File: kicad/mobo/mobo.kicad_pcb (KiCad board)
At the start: 4 copper layers, 22 x 58 mm, 47 parts, among them J1 HRO_TYPE-C-31-M-14, J2 Battery, J3 rgb, J4 columns, J5 Conn_01x10, J6 rows, J7 sensor, Q1 AO3401A, Q2 2N7002, SW1 Battery, SW2 Reset, U1 BQ24075, U2 nRF52840_E73-2G4M08S1C, Y1 32.768 KHz

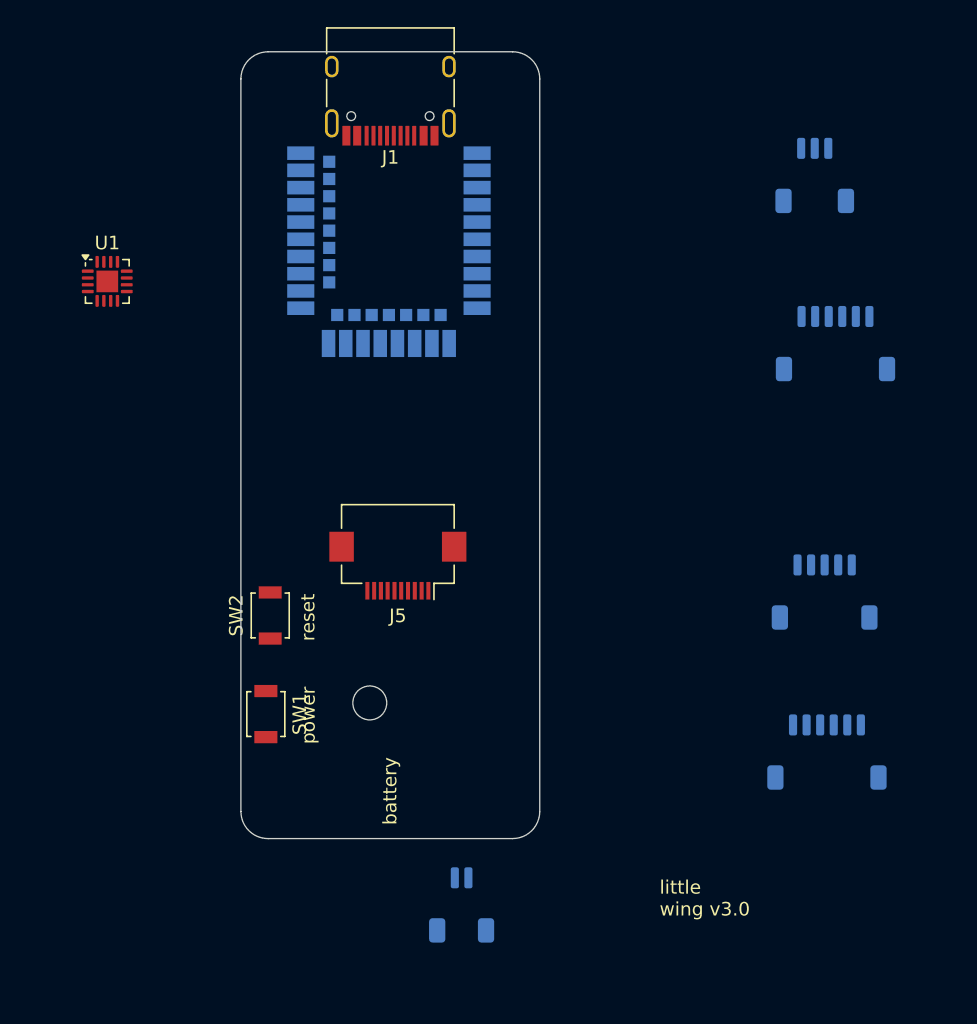
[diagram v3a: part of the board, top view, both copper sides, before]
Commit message: Adding connectors 3d files
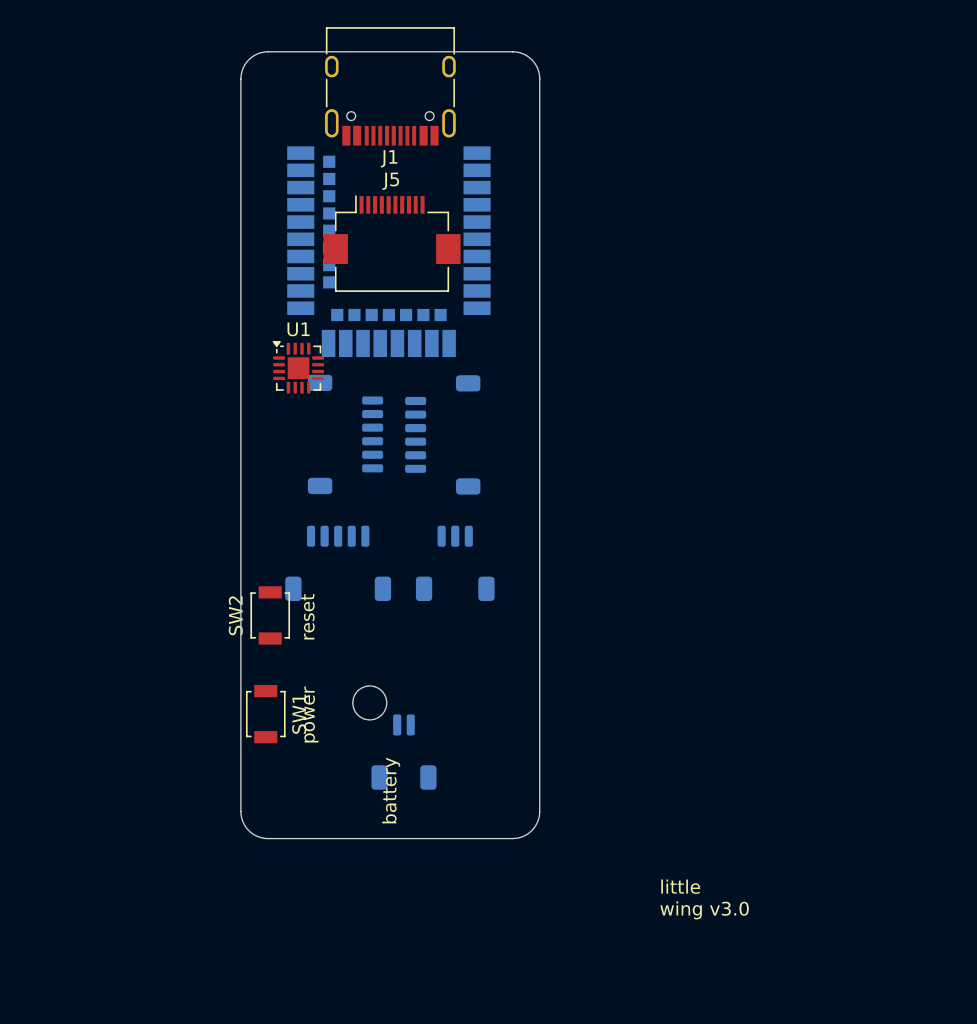
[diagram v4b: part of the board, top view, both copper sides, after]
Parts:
- moved J7 42.5 mm to (189.8, 60.2), turned to 90 degrees
- moved J3 39.0 mm to (197.8, 69.7)
- moved J6 35.9 mm to (189.2, 69.7)
- moved J4 29.7 mm to (196.9, 60.2), turned to -90 degrees
- moved J5 24.7 mm to (193.2, 45.1), turned to 0 degrees
- moved U1 15.5 mm to (186.3, 55.3)
- moved J2 12.0 mm to (194.1, 83.6)

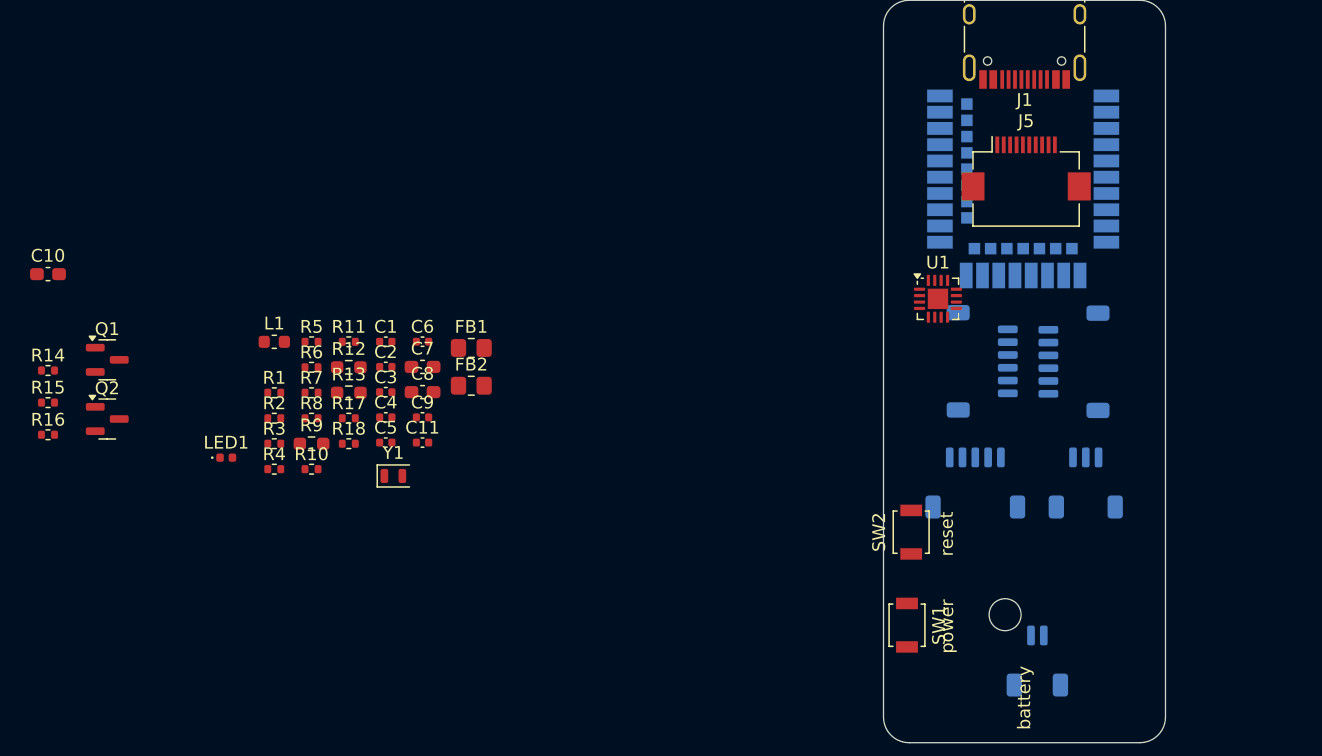
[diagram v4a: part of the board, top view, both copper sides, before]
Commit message: Assigning all the perifery pins
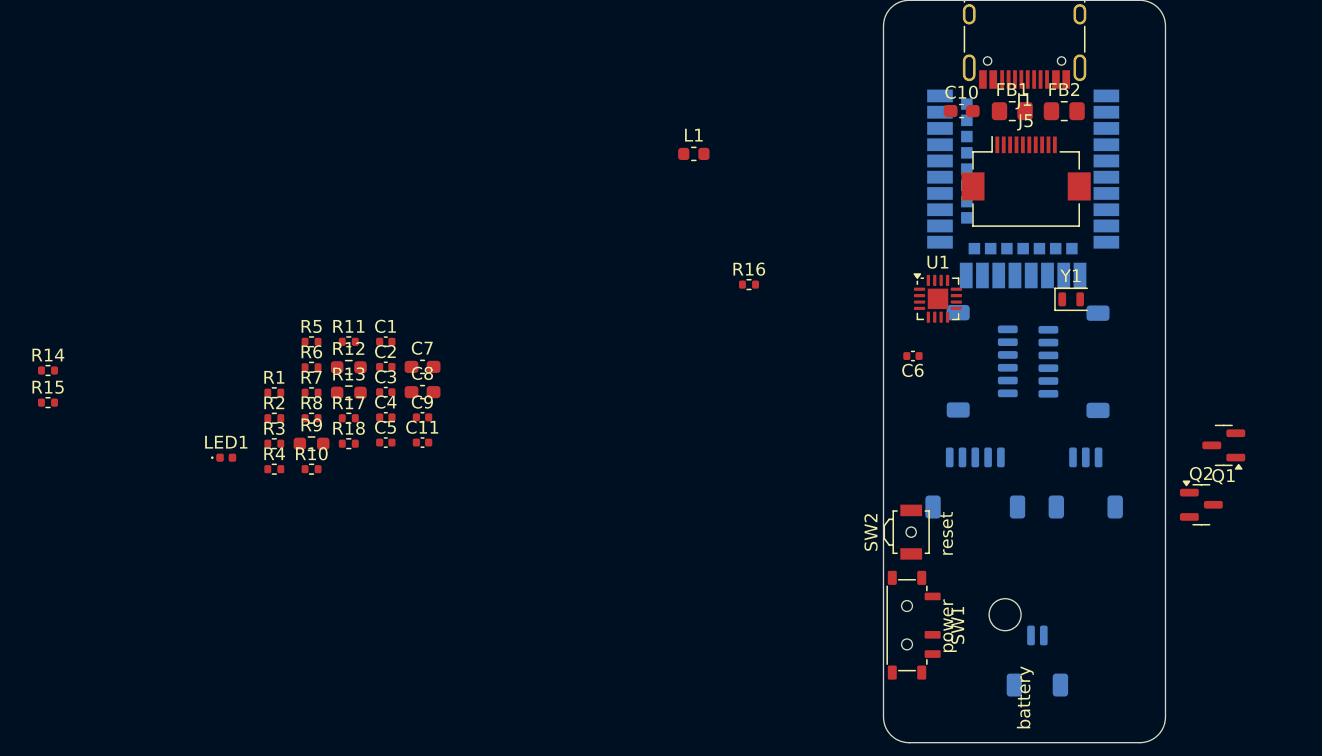
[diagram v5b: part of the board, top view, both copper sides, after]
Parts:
- SW1: footprint Button_Switch_SMD:SW_SPST_B3U-1000P -> ScottoKeebs_Components:Switch_MSK12C02
- SW2: footprint Button_Switch_SMD:SW_SPST_B3U-1000P -> Button_Switch_SMD:SW_SPST_B3U-3000P-B
- moved Q1 87.5 mm to (208.6, 66.8), turned to 180 degrees
- moved Q2 85.7 mm to (206.9, 71.4)
- moved C10 72.5 mm to (188.1, 40.7)
- moved R16 56.0 mm to (171.5, 54.2)
- moved Y1 54.7 mm to (196.7, 55.4)
- moved FB2 51.1 mm to (196.2, 40.7)
- moved FB1 46.1 mm to (192.1, 40.7)
- moved C6 38.3 mm to (184.3, 59.8), turned to 180 degrees
- moved L1 35.9 mm to (167.2, 44.0)
- turned SW1 to 90 degrees

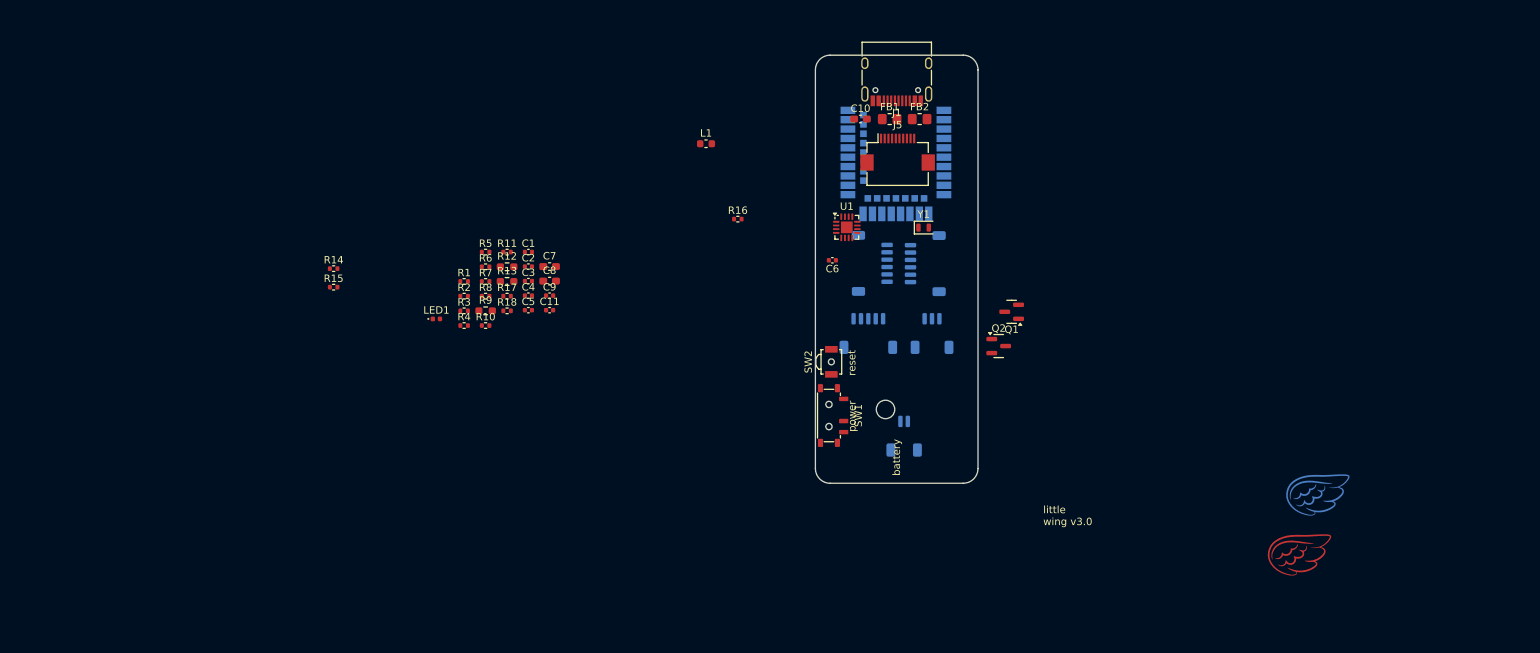
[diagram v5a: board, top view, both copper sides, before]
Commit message: Groupping around the PCB components
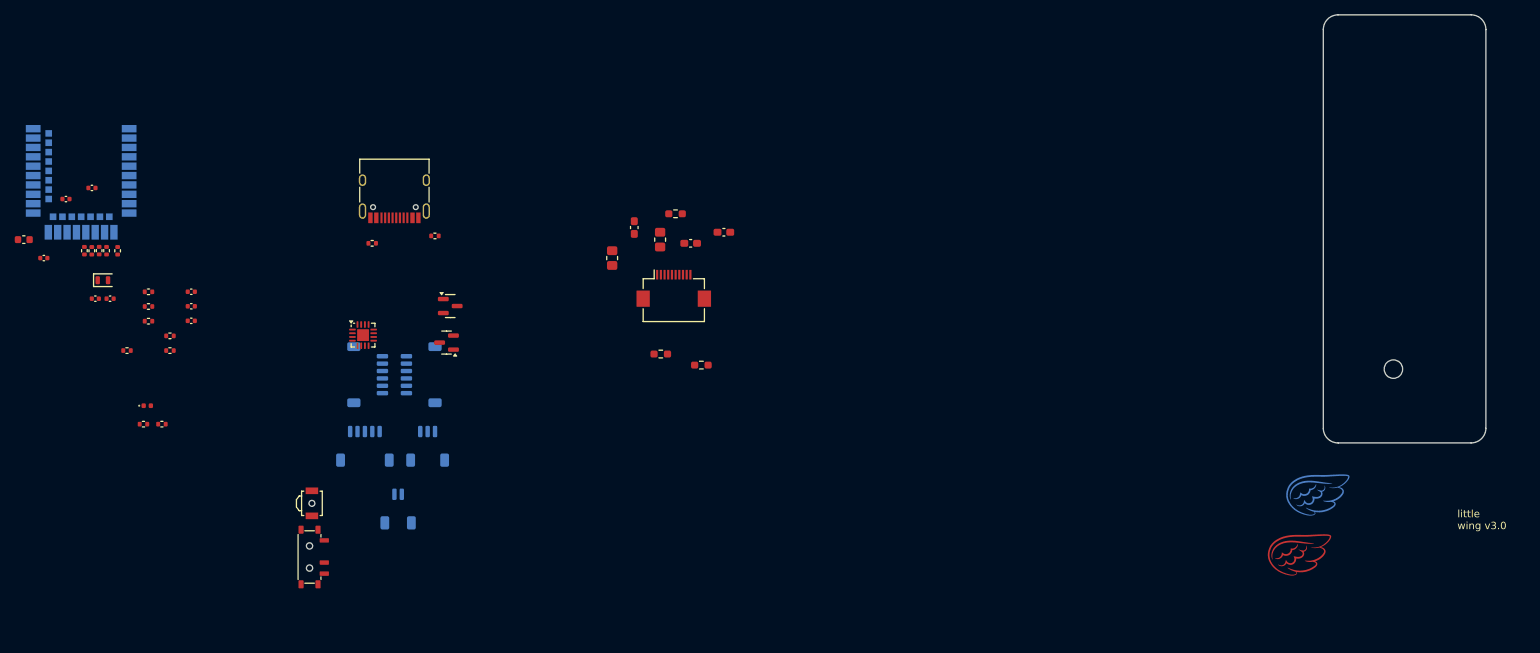
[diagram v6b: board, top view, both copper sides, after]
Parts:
- moved Y1 111.4 mm to (85.5, 62.5)
- moved U2 110.4 mm to (82.6, 47.0)
- moved C6 104.2 mm to (80.5, 51.5)
- moved L1 93.3 mm to (74.8, 57.0)
- moved R16 88.6 mm to (83.0, 58.5), turned to -90 degrees
- moved J4 77.0 mm to (121.4, 75.3), turned to 90 degrees
- moved Q1 76.7 mm to (132.1, 71.0)
- moved Q2 74.5 mm to (132.6, 66.0)
- moved SW1 72.9 mm to (113.5, 100.0)
- moved SW2 72.9 mm to (113.8, 92.7)
- moved J3 70.0 mm to (129.5, 85.0)
- moved J6 69.9 mm to (121.0, 85.0)
- moved J1 69.9 mm to (125.0, 50.0)
- moved J2 69.3 mm to (125.5, 93.5)
- moved U1 67.2 mm to (120.8, 69.9)
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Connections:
- J5 pad 2: LCD_IN -> LCD_DATA
- R11 pad 1: SESOR_CS -> SENSOR_CS
- R15 pad 1: SENSOR_SCK -> SENSOR_CLK
- U2 pad 12: unconnected-(U2-P0.26-Pad12) -> LCD_CS
- U2 pad 14: unconnected-(U2-P0.06-Pad14) -> LCD_DATA
- U2 pad 15: unconnected-(U2-P0.05/AIN3-Pad15) -> LCD_CLK
- U2 pad 16: unconnected-(U2-P0.08-Pad16) -> SENSOR_CS
- U2 pad 18: unconnected-(U2-P0.04/AIN2-Pad18) -> SENSOR_SDIO
- U2 pad 20: unconnected-(U2-P0.12-Pad20) -> SENSOR_CLK
- U2 pad 22: unconnected-(U2-P0.07-Pad22) -> SENSOR_IRQ
- U2 pad 28: unconnected-(U2-P0.15-Pad28) -> Row 5
- U2 pad 30: unconnected-(U2-P0.17-Pad30) -> Row 4
- U2 pad 32: unconnected-(U2-P0.20-Pad32) -> Row 3
- U2 pad 33: unconnected-(U2-P0.13-Pad33) -> Row 2
- U2 pad 34: unconnected-(U2-P0.22-Pad34) -> Row 1
- U2 pad 35: unconnected-(U2-P0.24-Pad35) -> Row 0
- U2 pad 36: RGB_ON -> Col 5
- U2 pad 38: unconnected-(U2-P1.02-Pad38) -> Col 4
- U2 pad 40: unconnected-(U2-P1.04-Pad40) -> Col 3
- U2 pad 41: unconnected-(U2-P0.09/NFC1-Pad41) -> Col 2
- U2 pad 42: unconnected-(U2-P1.06-Pad42) -> Col 1
- U2 pad 43: unconnected-(U2-P0.10/NFC2-Pad43) -> Col 0
- U2 pad 7: unconnected-(U2-P0.02/AIN0-Pad7) -> RGB_DATA
- U2 pad 8: unconnected-(U2-P0.29/AIN5-Pad8) -> RGB_ON
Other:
- board text removed: "battery"
- board text removed: "power"
- board text removed: "reset"

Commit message: Loosely optimising the groups components placement
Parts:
- added SW1: Battery, ScottoKeebs_Components:Switch_MSK12C02, F.Cu at (134.0, 100.0)
- added SW2: Reset, Button_Switch_SMD:SW_SPST_B3U-3000P-B, F.Cu at (134.0, 92.7)
- FB1, FB2: value Ferrite_Bead_Small -> 2.7k; footprint Resistor_SMD:R_0805_2012Metric_Pad1.20x1.40mm_HandSolder -> Resistor_SMD:R_0603_1608Metric
- R12, R13, R9: footprint Resistor_SMD:R_0603_1608Metric_Pad0.98x0.95mm_HandSolder -> Resistor_SMD:R_0402_1005Metric
- moved R2 56.9 mm to (76.0, 40.0)
- moved R10 53.3 mm to (146.5, 76.5), turned to -90 degrees
- moved R18 52.5 mm to (146.5, 80.0), turned to 90 degrees
- moved J1 44.6 mm to (82.5, 36.5)
- moved R1 37.3 mm to (89.0, 40.0)
- moved U1 24.3 mm to (96.4, 68.8)
- moved R17 20.0 mm to (87.0, 51.5), turned to -90 degrees
- moved Q2 18.2 mm to (144.1, 80.0), turned to 180 degrees
- moved C7 14.6 mm to (162.0, 68.5), turned to -90 degrees
- moved R9 14.5 mm to (163.5, 68.0), turned to 90 degrees
- moved FB1 13.8 mm to (165.0, 68.5), turned to -90 degrees
- moved R4 13.8 mm to (100.0, 71.5)
- moved C10 13.2 mm to (156.0, 68.5), turned to -90 degrees
- moved Q1 13.2 mm to (144.1, 76.5)
- moved C8 11.9 mm to (160.5, 68.5), turned to -90 degrees
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
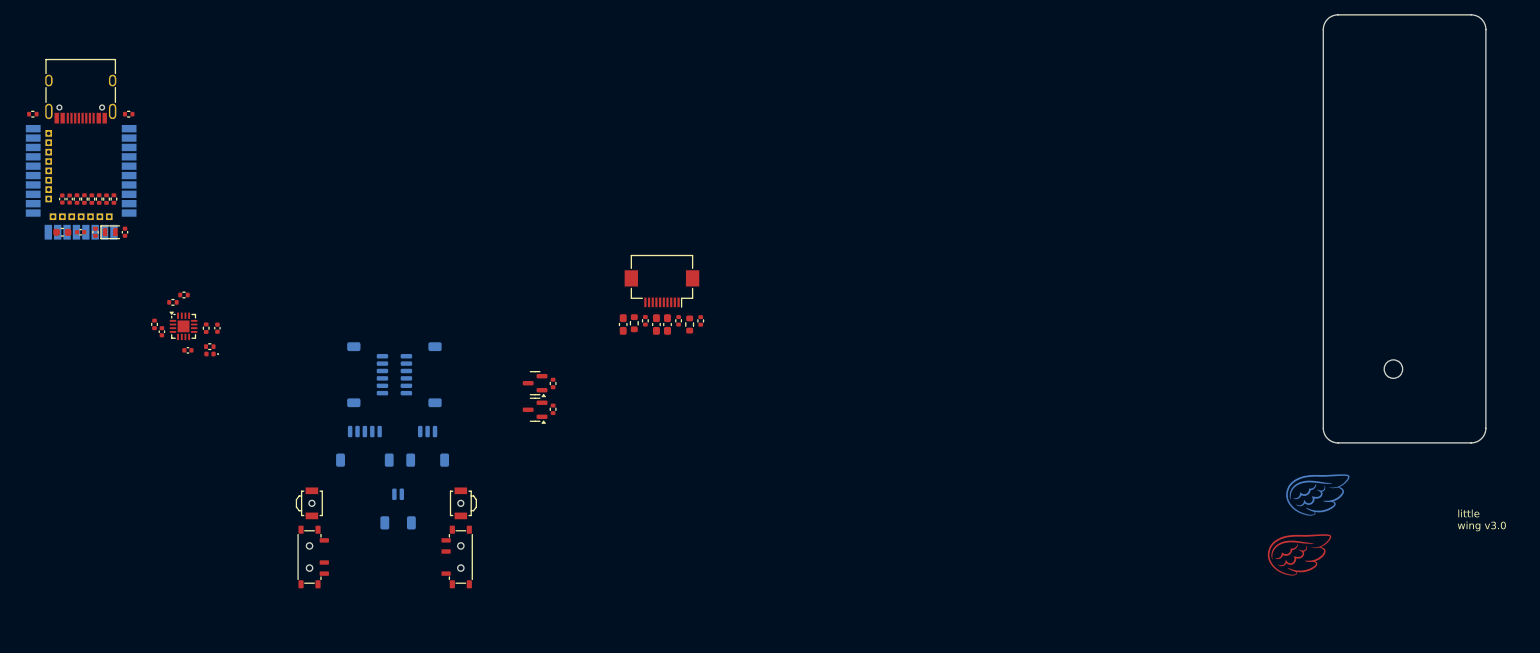
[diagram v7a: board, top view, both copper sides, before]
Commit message: Groupping the groups into a workable arrangement
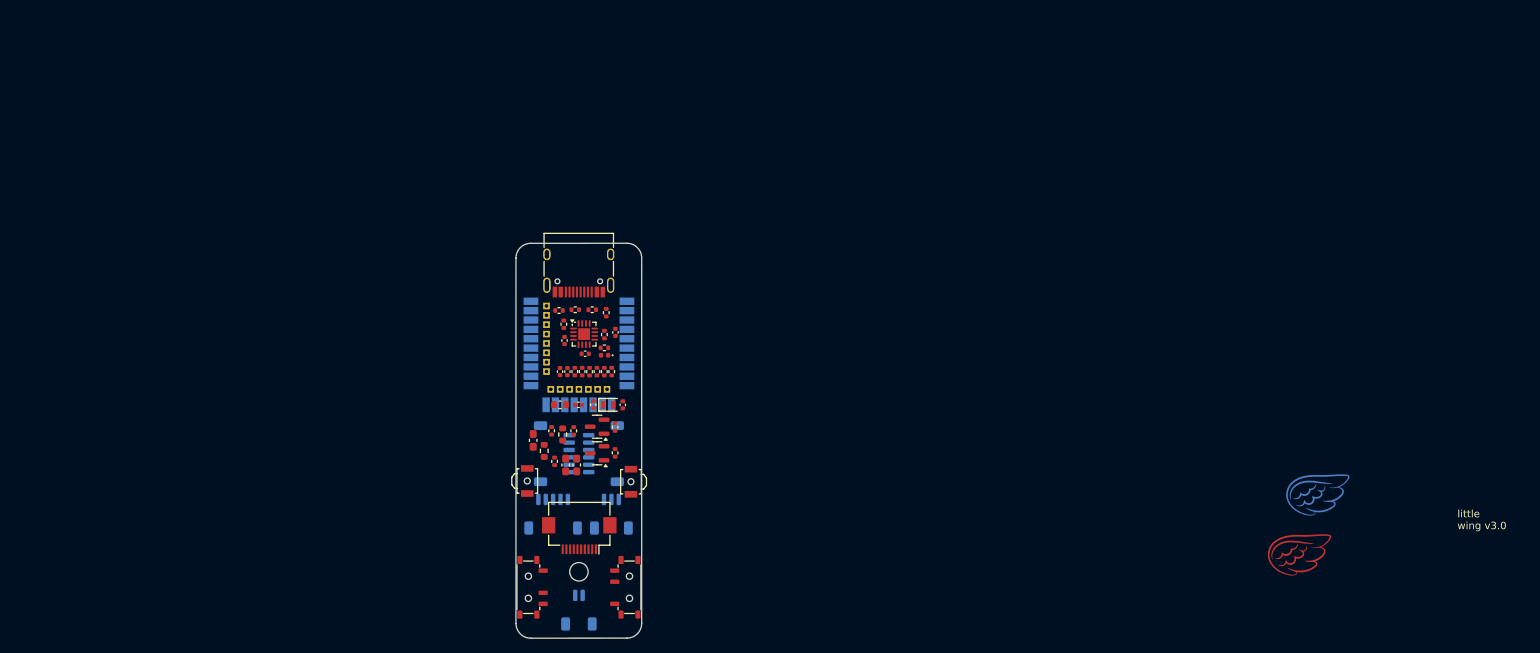
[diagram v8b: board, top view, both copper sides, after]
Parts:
- moved R2 76.1 mm to (147.3, 66.6)
- moved J1 71.5 mm to (150.0, 60.0)
- moved C11 71.4 mm to (151.9, 79.4)
- moved C4 71.4 mm to (149.9, 79.4)
- moved C5 71.4 mm to (147.4, 74.9)
- moved C6 71.4 mm to (148.4, 74.9), turned to -90 degrees
- moved C9 71.4 mm to (155.9, 79.4)
- moved L1 71.4 mm to (147.4, 79.4)
- moved R11 71.4 mm to (152.4, 74.9)
- moved R14 71.4 mm to (151.4, 74.9)
- moved R15 71.4 mm to (150.4, 74.9)
- moved R16 71.4 mm to (149.4, 74.9)
- moved R17 71.4 mm to (154.4, 74.9)
- moved R8 71.4 mm to (153.4, 74.9)
- moved U2 71.4 mm to (150.0, 70.4)
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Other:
- board size 22 x 58 mm -> 17 x 53.5 mm
